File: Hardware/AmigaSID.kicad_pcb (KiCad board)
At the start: 2 copper layers, 130 x 67.5 mm, 42 parts, among them CON1 ZorroII, J1 AudioJack3, J2 SID_AUDIO_OUT, J3 SID_AUDIO_IN, Q1 BC547, U1 74HC688, U2 74LS00, U3 SID, U4 LM7809_TO220, U5 74HC245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

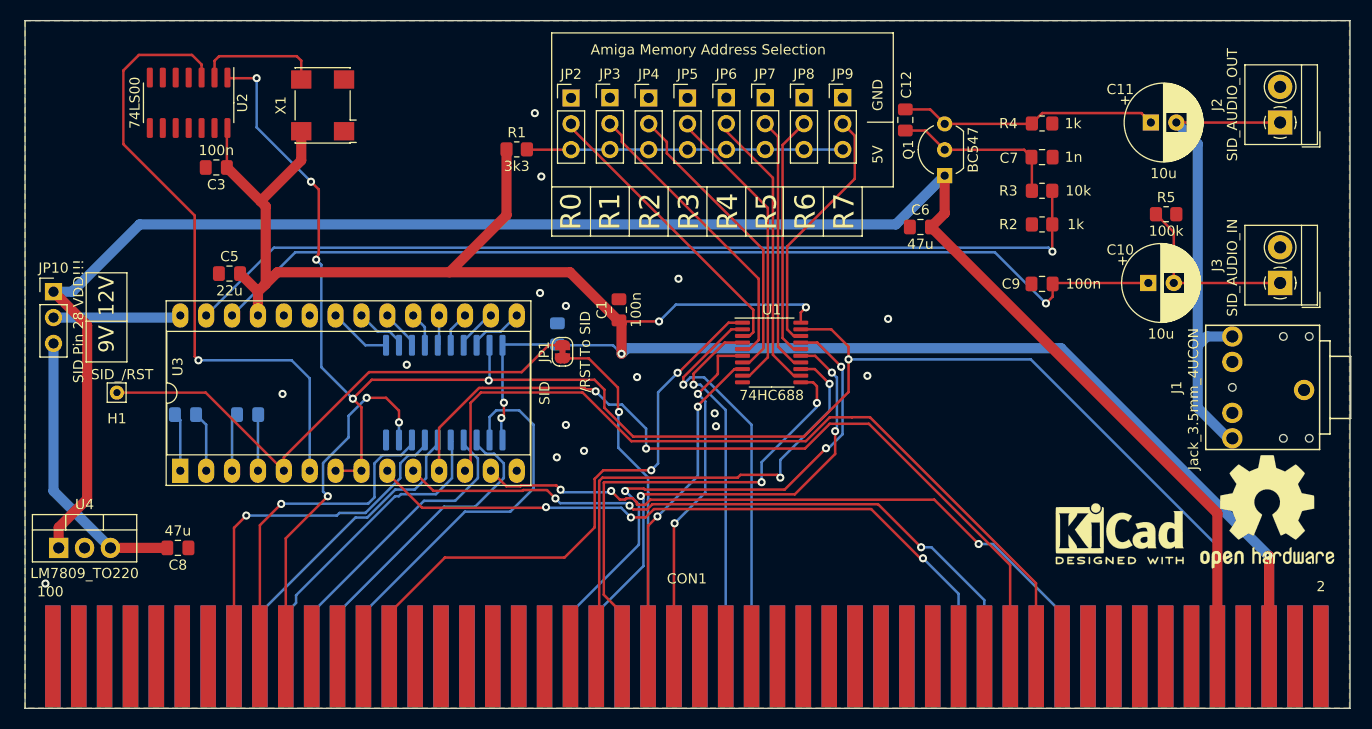
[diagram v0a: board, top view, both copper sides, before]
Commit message: - Moved filter caps closer to IC's - Added logo - Floating 245 inputs tied to VCC - Flipped polarity on C10 (SID_AUDIO_IN) - Added jumper to disconnect audio out cap from output pins   - instead you now can fit a little amp board like shown Gadgets video about the original version of the card   - also added one GND and one 12V pin
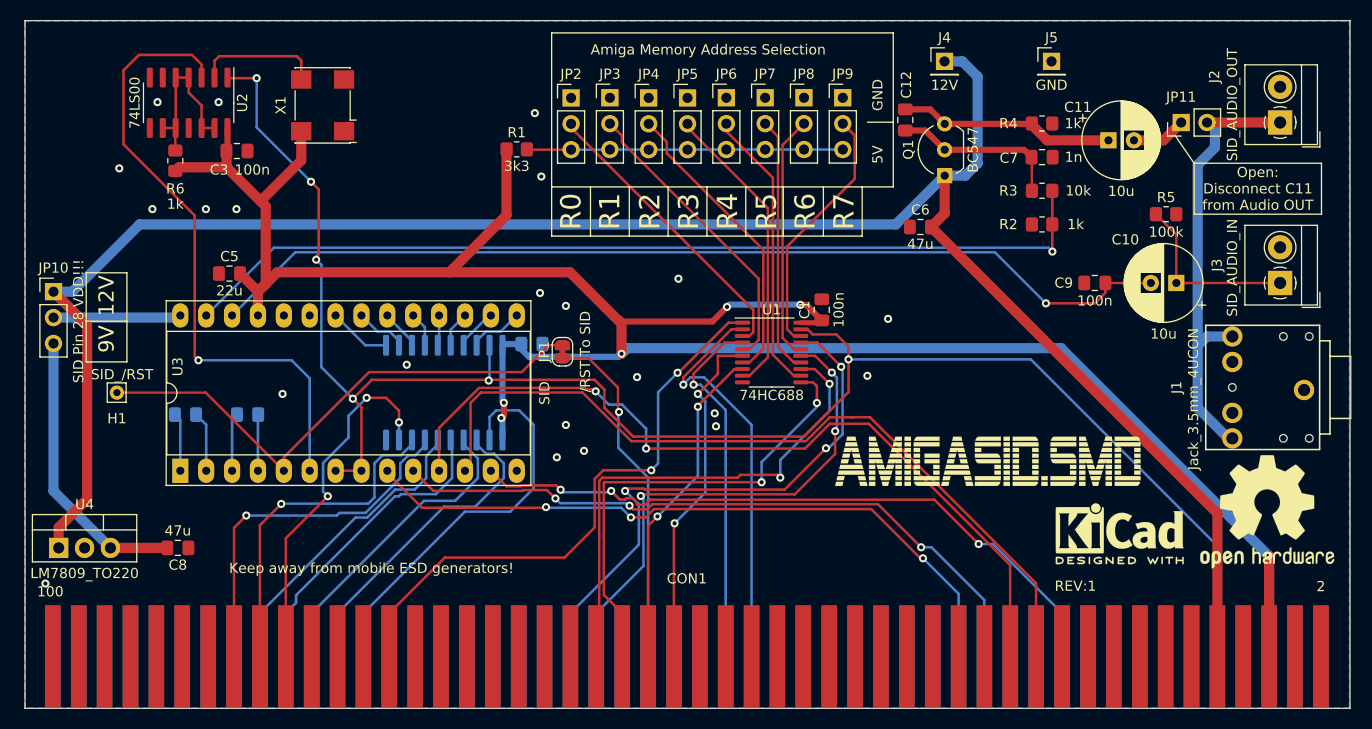
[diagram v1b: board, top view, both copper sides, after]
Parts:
- added J4: 12V, Connector_PinHeader_2.54mm:PinHeader_1x01_P2.54mm_Vertical, F.Cu at (174.1, 71.4)
- added J5: GND, Connector_PinHeader_2.54mm:PinHeader_1x01_P2.54mm_Vertical, F.Cu at (184.6, 71.4)
- added JP11: Disconnect C11 from Audio OUT, Connector_PinHeader_2.54mm:PinHeader_1x02_P2.54mm_Vertical, F.Cu at (197.3, 77.4)
- added R6: 1k, Resistor_SMD:R_0805_2012Metric_Pad1.20x1.40mm_HandSolder, F.Cu at (98.6, 81.1)
- added REF**: AmigaSID.SMD, AmigaSID:AmigaSID.SMD, F.Cu at (178.3, 110.6)
- added REF**: AsSeenOn, AmigaSID:AsSeenOn, B.Cu at (149.3, 109.1)
- added REF**: t_o_i, AmigaSID:t_o_i, B.Cu at (184.6, 109.9)
- moved C1 19.9 mm to (162.0, 95.8)
- moved C9 5.18 mm to (188.8, 93.1)
- moved C11 4.51 mm to (190.2, 79.1)
- moved C10 2.75 mm to (196.8, 93.1), turned to 180 degrees
- moved C13 2.69 mm to (133.6, 99.1), turned to 0 degrees
- moved C3 2.59 mm to (104.6, 80.2), turned to 0 degrees
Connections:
- C10 pad 1: /SID_EXT_IN -> Net-(C10-Pad1)
- C10 pad 2: Net-(C10-Pad2) -> /SID_EXT_IN
- J1 pad R: Net-(C11-Pad2) -> Net-(J1-PadR)
- J1 pad T: Net-(C11-Pad2) -> Net-(J1-PadR)
- J2 pad 1: Net-(C11-Pad2) -> Net-(J1-PadR)
- J3 pad 1: Net-(C10-Pad2) -> Net-(C10-Pad1)
- R5 pad 1: Net-(C10-Pad2) -> Net-(C10-Pad1)
- U2 pad 10: unconnected-(U2-Pad10) -> Net-(R6-Pad2)
- U2 pad 12: unconnected-(U2-Pad12) -> Net-(R6-Pad2)
- U2 pad 13: unconnected-(U2-Pad13) -> Net-(R6-Pad2)
- U2 pad 4: unconnected-(U2-Pad4) -> Net-(R6-Pad2)
- U2 pad 5: unconnected-(U2-Pad5) -> Net-(R6-Pad2)
- U2 pad 9: unconnected-(U2-Pad9) -> Net-(R6-Pad2)
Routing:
- net Net-(J1-PadR): track 0.00 -> 43.9 mm
- net Net-(C11-Pad2): track 47.1 -> 5.36 mm
- net Net-(C10-Pad2): track 17.9 -> 0.00 mm
- net Net-(C10-Pad1): track 0.00 -> 17.8 mm
- net Net-(R6-Pad2): track 0.00 -> 16.5 mm
- net /12v: track 179.2 -> 195.4 mm
- net +5V: track 220.7 -> 228.5 mm
- net Net-(C12-Pad2): track 25.5 -> 21.3 mm
- net GND: vias 16 -> 22
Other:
- board text added: "Keep away from mobile ESD generators!"
- board text added: "Open: Disconnect C11 from Audio OUT"
- board text added: "REV:1"
